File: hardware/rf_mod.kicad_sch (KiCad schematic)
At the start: 170 parts, among them J1001 SMA, J1002 SMA, J1003 Pmod, J101 SMA, J102 SMA, J103 SMA, J1201 SMA, J1202 SMA, J1301 SMA, J1302 SMA, J1303 SMA, J201 SMA, J202 SMA, J401 SMA, J402 SMA, J501 SMA, J502 SMA, J701 SMA, J702 SMA, J703 SMA, J801 SMA, J802 SMA, J803 SMA, J901 USB-C, J902 SMA, Q1001 AO3401A, Q1201 AO3401A, Q1301 AO3401A, Q501 AO3401A, Q701 AO3401A, Q801 AO3401A, SW1001 ON, SW1201 ON, SW1301 ON, SW501 ON, SW701 ON, SW801 ON, U1001 3.3V, U1002 MAX2871, U1201 GALI-84+, U1301 TRF3722, U1302 3.3V, U501 QPL9547, U701 3.3V, U702 ADL5350, U801 3.3V, U802 ADL5350, U901 MT3608, U902 3.3V, U903 74LVC1G17, X901 25 MHz

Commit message: RF-MOD: R1 is a diode-ring mixer (ADEX-10L+, 10-1000 MHz, LO +4 dBm; its baluns and ring of four diodes drawn on the silk) in the splitter's place; R10's RFOUTA- comes out on OUT A- (bottom-right of its right cell) along a 50 ohm line in the margin under the tile, the top pour following it; OUT A becomes OUT A+
Generators: silk drawings (Tile.draw_line / draw_arc), a top-pour tongue below an RF tile (Tile.pour_below), jack names slide up to 4.5 mm and say what blocks them; footprints, symbols and models for the ADEX-10L+ and the HHM22137A1 coupler.

Co-Authored-By: Claude Opus 5.5 <noreply@anthropic.com>
Claude-Session: https://claude.ai/code/session_01RKeoKvFFzjk3cEBLCXXHnB
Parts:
- removed R1006: 5.1k, Resistor_SMD:R_0402_1005Metric, symbol Device:R_US
- removed R101, R102, R103: 18R, Resistor_SMD:R_0402_1005Metric, symbol Device:R_US
- added J1004: Pmod, amod:PinHeader_2x06_P2.54mm_Horizontal_PZ254R-12-12P, symbol Connector_Generic:Conn_02x06_Odd_Even
- added U101: ADEX-10L+, amod:MiniCircuits_CD542_ADEX-10L, symbol amod:ADEX10L
- J1003: value Pmod -> SMA; footprint amod:PinHeader_2x06_P2.54mm_Horizontal_PZ254R-12-12P -> amod:SMA_BWSMA-KE-Z001_Vertical; symbol Connector_Generic:Conn_02x06_Odd_Even -> Connector:Conn_Coaxial; LCSC C492434 -> C496549; MPN PZ254R-12-12P -> BWSMA-KE-Z001
- R1005: value 51R -> 5.1k; LCSC C25125 -> C25905; MPN 0402WGF510JTCE -> 0402WGF5101TCE
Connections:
- net GND: now also J1003.2 (Ext), J1004.3 (Pin_3), J1004.4 (Pin_4), U101.1 (GND), U101.4 (GND), U101.5 (GND); no longer J1003.3 (Pin_3), J1003.4 (Pin_4)
- net PMOD1: now also J1004.12 (Pin_12); no longer J1003.12 (Pin_12)
- net PMOD2: now also J1004.10 (Pin_10); no longer J1003.10 (Pin_10)
- net PMOD3: now also J1004.8 (Pin_8); no longer J1003.8 (Pin_8)
- net PMOD4: now also J1004.6 (Pin_6); no longer J1003.6 (Pin_6)
- net PMOD5: now also J1004.11 (Pin_11); no longer J1003.11 (Pin_11)
- net PMOD6: now also J1004.9 (Pin_9); no longer J1003.9 (Pin_9)
- net PMOD_VCC: now also J1004.1 (Pin_1), J1004.2 (Pin_2); no longer J1003.1 (Pin_1), J1003.2 (Pin_2)
- net R10_RS: now also R1005.1
- net R10_TRM renamed R10_OUTAN
- net R10_OUTAN: now also J1003.1 (In); no longer R1005.1
- net R1_P1 renamed R1_LO
- net R1_LO: now also U101.6 (LO)
- net R1_P2 renamed R1_RF
- net R1_RF: now also U101.3 (RF)
- net R1_P3 renamed R1_IF
- net R1_IF: now also U101.2 (IF)
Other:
- note added: "(+4 dBm, +1 to +7) turns the diodes on in pairs, so the RF is multiplied by +-1 at the LO rate: the IF is RF x square"
- note added: "+4 dBm"
- note added: "-5 dBm"
- note added: "3.3 V and 100 pF: two outputs, 180 degrees apart; put a 50 ohm terminator on one that is unused. RFOUTB is open and must"
- note added: "EXPECT: about 7 dB of conversion loss from 10 MHz to 1 GHz with +4 dBm of LO (R10 at its top power), IF from DC to 800 MHz, 60 dB L-R isolation"
- note added: "EXPECT: any frequency from 23.5 MHz to 6 GHz on OUT A+ and OUT A- (each -4 to +5 dBm in steps, 180 degrees apart), locked to the 25 MHz on REF IN; the red LED says locked"
- note added: "Mini-Circuits ADEX-10L+: two wideband baluns and a ring of four Schottky diodes (drawn beside it on the silk). The LO"
- note added: "OUT A+"
- note added: "OUT A-"
- note added: "R1 diode mixer, ADEX-10L+"
- note added: "REF OUT (51 ohm: 1.6 Vpp into 50 ohm, 3.3 Vpp into a synthesizer's unterminated REF IN; R10's REF IN passes it to R13)."
- note added: "a frequency); 1 dB compression at +1 dBm of RF, IP3 +16 dBm. Compare R7/R8 (ADL5350) and AMOD-A's A9 (MC1496)."
- note added: "and 2.4 GHz (VCO / 2) at ICP 2.56 mA (RSET 5.1 k, CP = 7). RFOUTA+ and RFOUTA- each feed a jack through 27 nH to"
- note added: "stay disabled. CE and RFOUT_EN are tied high, LE has 100 k down. REF IN is unterminated; a back trace takes it on to R13."
- note added: "wave, the sum and difference plus odd LO harmonics. Passive and DC-coupled at IF (a phase detector when RF and LO share"
- note removed: "+20 dBm"
- note removed: "100 pF; RFOUTA- is terminated in 51 ohm the same way; RFOUTB is open and must stay disabled. CE and RFOUT_EN are"
- note removed: "EXPECT: 6.2 dB from any port to either other port, every port within 2 ohm of 50, DC to 6 GHz (the resistors' parasitics set the top)"
- note removed: "EXPECT: any frequency from 23.5 MHz to 6 GHz on OUT A (-4 to +5 dBm in steps), locked to the 25 MHz on REF IN; the red LED says locked"
- note removed: "OUT A"
- note removed: "P1"
- note removed: "P2"
- note removed: "P3"
- note removed: "R1 splitter, 3 x 18 ohm, 6 dB"
- note removed: "REF OUT (51 ohm: 1.6 Vpp into 50 ohm, 3.3 Vpp into a synthesizer's unterminated REF IN; R1 feeds both synthesizers)."
- note removed: "Three 18 ohm resistors to one node: the textbook resistive divider, 6 dB per path and no isolation between the two"
- note removed: "and 2.4 GHz (VCO / 2) at ICP 2.56 mA (RSET 5.1 k, CP = 7). RFOUTA+ feeds the jack through 27 nH to 3.3 V and"
- note removed: "both synthesizers' REF IN, one synthesizer's OUT A to both mixers, or two tones into one gain block."
- note removed: "outputs beyond those 6 dB (a Wilkinson would give 3 dB and 20 dB of isolation, at one band). Feed R9's REF OUT to"
- note removed: "tied high, LE has 100 k down. REF IN is unterminated: one REF OUT drives both synthesizers through R1."
- moved on the sheet: C1011, C1012, C1013, C1014, C1015, J102, J103, R1005

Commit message: Silk case convention on all six boards (Jason, Prompt 17: "To distinguish whole-tile labels from SMA or port labels, use different cases")
Ports (the jacks' names, terminal and loop names, a port named inside a note) stay UPPER CASE.  A tile's label (its
title on the frame, its name in the corner) is Mixed case: the first letter capitalised and the rest as written ("RC
low-pass", "Synthesizer", "I/Q demodulator"; tiles.label_case).  Ranges, values and notes are lower case except units,
acronyms and part numbers ("loss 1.7 dB", "OUT floats").  RF-MOD-2's X1 and X2 take word titles with their chips in
the info; RF-MOD's and RF-MOD-2's LNA tiles are titled "Preamp" ("Low-noise amp" does not fit a cell's frame); a few
two-line labels moved 0.15-0.3 mm for the descenders mixed case brings.  AMOD-P2's tile records (tile_docs), its DOA
list, KIT.md's AMOD-P2 section; X5's calibration points at P14.  All six boards: ERC 0, DRC 0, all fab checks.

Co-Authored-By: Claude Opus 5.5 <noreply@anthropic.com>
Claude-Session: https://claude.ai/code/session_01RKeoKvFFzjk3cEBLCXXHnB
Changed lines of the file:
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@@
 	(wire
 		(pts
+			(xy 370.84 441.96) (xy 365.76 441.96)
+		)
+		(stroke
+			(width 0)
+			(type default)
+		)
+	)
+	(wire
+		(pts
 			(xy 181.61 440.69) (xy 181.61 443.23)
 		)
@@
 	(wire
 		(pts
+			(xy 751.84 314.96) (xy 746.76 314.96)
+		)
+		(stroke
+			(width 0)
+			(type default)
+		)
+	)
+	(wire
+		(pts
 			(xy 167.64 336.55) (xy 170.18 336.55)
 		)
@@
 	(wire
 		(pts
+			(xy 180.34 187.96) (xy 175.26 187.96)
+		)
+		(stroke
+			(width 0)
+			(type default)
+		)
+	)
+	(wire
+		(pts
 			(xy 238.76 236.22) (xy 241.3 236.22)
 		)
@@
 	(wire
 		(pts
-			(xy 365.76 314.96) (xy 370.84 314.96)
-		)
-		(stroke
-			(width 0)
-			(type default)
-		)
-	)
-	(wire
-		(pts
 			(xy 756.92 193.04) (xy 756.92 195.58)
 		)
@@
 	(wire
 		(pts
+			(xy 751.84 187.96) (xy 746.76 187.96)
+		)
+		(stroke
+			(width 0)
+			(type default)
+		)
+	)
+	(wire
+		(pts
 			(xy 156.21 466.09) (xy 153.67 466.09)
 		)
@@
 	(wire
 		(pts
+			(xy 370.84 60.96) (xy 365.76 60.96)
+		)
+		(stroke
+			(width 0)
+			(type default)
+		)
+	)
+	(wire
+		(pts
 			(xy 566.42 66.04) (xy 566.42 68.58)
 		)
@@
 	(wire
 		(pts
+			(xy 345.44 441.96) (xy 340.36 441.96)
+		)
+		(stroke
+			(width 0)
+			(type default)
+		)
+	)
+	(wire
+		(pts
 			(xy 429.26 492.76) (xy 431.8 492.76)
 		)
@@
 	(wire
 		(pts
-			(xy 556.26 60.96) (xy 561.34 60.96)
-		)
-		(stroke
-			(width 0)
-			(type default)
-		)
-	)
-	(wire
-		(pts
 			(xy 519.43 450.85) (xy 521.97 450.85)
 		)
@@
 	(wire
 		(pts
+			(xy 751.84 60.96) (xy 746.76 60.96)
+		)
+		(stroke
+			(width 0)
+			(type default)
+		)
+	)
+	(wire
+		(pts
 			(xy 619.76 353.06) (xy 617.22 353.06)
 		)
@@
 	(wire
 		(pts
-			(xy 365.76 60.96) (xy 370.84 60.96)
-		)
-		(stroke
-			(width 0)
-			(type default)
-		)
-	)
-	(wire
-		(pts
 			(xy 424.18 441.96) (xy 429.26 441.96)
 		)
@@
 	(wire
 		(pts
-			(xy 365.76 187.96) (xy 370.84 187.96)
-		)
-		(stroke
-			(width 0)
-			(type default)
-		)
-	)
-	(wire
-		(pts
 			(xy 528.32 492.76) (xy 525.78 492.76)
 		)
@@
 	(wire
 		(pts
-			(xy 340.36 441.96) (xy 345.44 441.96)
-		)
-		(stroke
-			(width 0)
-			(type default)
-		)
-	)
-	(wire
-		(pts
 			(xy 607.06 500.38) (xy 609.6 500.38)
 		)
@@
 	(wire
 		(pts
-			(xy 175.26 187.96) (xy 180.34 187.96)
-		)
-		(stroke
-			(width 0)
-			(type default)
-		)
-	)
-	(wire
-		(pts
 			(xy 345.44 353.06) (xy 347.98 353.06)
 		)
@@
 	(wire
 		(pts
-			(xy 746.76 187.96) (xy 751.84 187.96)
-		)
-		(stroke
-			(width 0)
-			(type default)
-		)
-	)
-	(wire
-		(pts
 			(xy 190.5 223.52) (xy 193.04 223.52)
 		)
@@
 	(wire
 		(pts
-			(xy 746.76 60.96) (xy 751.84 60.96)
-		)
-		(stroke
-			(width 0)
-			(type default)
-		)
-	)
-	(wire
-		(pts
 			(xy 76.2 223.52) (xy 73.66 223.52)
 		)
@@
 	(wire
 		(pts
-			(xy 746.76 441.96) (xy 751.84 441.96)
-		)
-		(stroke
-			(width 0)
-			(type default)
-		)
-	)
-	(wire
-		(pts
 			(xy 368.3 500.38) (xy 370.84 500.38)
 		)
@@
 	(wire
 		(pts
+			(xy 561.34 60.96) (xy 556.26 60.96)
+		)
+		(stroke
+			(width 0)
+			(type default)
+		)
+	)
+	(wire
+		(pts
 			(xy 685.8 241.3) (xy 683.26 241.3)
 		)
@@
 	(wire
 		(pts
+			(xy 370.84 187.96) (xy 365.76 187.96)
+		)
+		(stroke
+			(width 0)
+			(type default)
+		)
+	)
+	(wire
+		(pts
 			(xy 129.54 199.39) (xy 132.08 199.39)
 		)
@@
 	(wire
 		(pts
+			(xy 370.84 314.96) (xy 365.76 314.96)
+		)
+		(stroke
+			(width 0)
+			(type default)
+		)
+	)
+	(wire
+		(pts
 			(xy 541.02 454.66) (xy 541.02 457.2)
 		)
@@
 	(wire
 		(pts
-			(xy 365.76 441.96) (xy 370.84 441.96)
-		)
-		(stroke
-			(width 0)
-			(type default)
-		)
-	)
-	(wire
-		(pts
 			(xy 535.94 492.76) (xy 538.48 492.76)
 		)
@@
 	(wire
 		(pts
-			(xy 706.12 492.76) (xy 703.58 492.76)
+			(xy 751.84 441.96) (xy 746.76 441.96)
 		)
 		(stroke
@@
 	(wire
 		(pts
-			(xy 429.26 500.38) (xy 431.8 500.38)
+			(xy 706.12 492.76) (xy 703.58 492.76)
 		)
 		(stroke
@@
 	(wire
 		(pts
-			(xy 274.32 223.52) (xy 276.86 223.52)
+			(xy 429.26 500.38) (xy 431.8 500.38)
 		)
 		(stroke
@@
 	(wire
 		(pts
-			(xy 627.38 241.3) (xy 629.92 241.3)
+			(xy 274.32 223.52) (xy 276.86 223.52)
 		)
 		(stroke
@@
 	(wire
 		(pts
-			(xy 520.7 353.06) (xy 518.16 353.06)
+			(xy 627.38 241.3) (xy 629.92 241.3)
 		)
 		(stroke
@@
 	(wire
 		(pts
-			(xy 520.7 254) (xy 518.16 254)
+			(xy 520.7 353.06) (xy 518.16 353.06)
 		)
 		(stroke
@@
 	(wire
 		(pts
-			(xy 449.58 314.96) (xy 454.66 314.96)
+			(xy 520.7 254) (xy 518.16 254)
 		)
 		(stroke
@@
 	(wire
 		(pts
-			(xy 88.9 457.2) (xy 86.36 457.2)
+			(xy 449.58 314.96) (xy 454.66 314.96)
 		)
 		(stroke
@@
 	(wire
 		(pts
-			(xy 746.76 314.96) (xy 751.84 314.96)
+			(xy 88.9 457.2) (xy 86.36 457.2)
 		)
 		(stroke

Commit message: One letter per board, tiles in lower case: AMOD-P2 is AMOD-N (n1-n11), RF-MOD-2 is IQ-MOD (q1-q11), PhMOD's tiles h1-h10
Jason, Prompt 19: "If we can have a nice, well justified single-letter designator for each board, it would make
everything much more clear", and "d11, q11, and c11 don't look like obvious electronics or PCB things".

- p passive, n networks (AMOD-P2's P14, P16-P25), a active, r radio, h PhMOD (Y1-Y10), q quadrature (RF-MOD-2's X1-X11);
  c, m and b are taken for the conversion, motor and brushless boards to come.  PLAN.md section 13 has the table and
  the reasons (no letter moves to another board, no retired name is reused, no s: s11 is the reflection coefficient).
- Every tile name in lower case on the silk, in the code (Tile ids, BACK/BACK_PLOTS/DOCS keys, the nets built on them),
  the handbooks, README, DOA lists, KIT, PLAN and the review brief; pin names (USB-C A1...), the 4046's R1/C1, nets
  named N1/P1, part numbers ending -R7 and the paper size A1 left alone.  tiles.dump refuses a tile not named
  <letter><n>, a number twice, and a BACK key for a tile that does not exist.
- Board and file renames: boards/amod_n.py, boards/iq_mod.py, docs/DOA_amod_n.md, docs/DOA_iq_mod.md, the handbooks,
  the generated hardware, outputs and pictures.  Silk nudged where a lower-case p or q hung onto the line below.
- All six boards rebuilt: ERC 0, DRC 0, every check.

Co-Authored-By: Claude Opus 5.5 <noreply@anthropic.com>
Claude-Session: https://claude.ai/code/session_01RKeoKvFFzjk3cEBLCXXHnB
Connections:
- net R10_AN renamed r10_AN
- net R10_AP renamed r10_AP
- net R10_BF renamed r10_BF
- net R10_CP renamed r10_CP
- net R10_G renamed r10_G
- net R10_LD renamed r10_LD
- net R10_LEDA renamed r10_LEDA
- net R10_N2 renamed r10_N2
- net R10_NF renamed r10_NF
- net R10_OUTA renamed r10_OUTA
- net R10_OUTAN renamed r10_OUTAN
- net R10_REFI renamed r10_REFI
- net R10_REG renamed r10_REG
- net R10_RS renamed r10_RS
- net R10_TN renamed r10_TN
- net R10_V33 renamed r10_V33
- net R10_VS renamed r10_VS
- net R12_G renamed r12_G
- net R12_IN renamed r12_IN
- net R12_IN_A renamed r12_IN_A
- net R12_OUT renamed r12_OUT
- net R12_OUT_A renamed r12_OUT_A
- net R12_VD renamed r12_VD
- net R12_VS renamed r12_VS
- net R13_BBI renamed r13_BBI
- net R13_BBQ renamed r13_BBQ
- net R13_BIN renamed r13_BIN
- net R13_BIP renamed r13_BIP
- net R13_BQN renamed r13_BQN
- net R13_BQP renamed r13_BQP
- net R13_CP renamed r13_CP
- net R13_G renamed r13_G
- net R13_LD renamed r13_LD
- net R13_LEDA renamed r13_LEDA
- net R13_N2 renamed r13_N2
- net R13_REFI renamed r13_REFI
- net R13_RFO renamed r13_RFO
- net R13_RFOUT renamed r13_RFOUT
- net R13_V33 renamed r13_V33
- net R13_VS renamed r13_VS
- net R13_VT renamed r13_VT
- net R1_IF renamed r1_IF
- net R1_LO renamed r1_LO
- net R1_RF renamed r1_RF
- net R2_IN renamed r2_IN
- net R2_OUT renamed r2_OUT
- net R4_IN renamed r4_IN
- net R4_OUT renamed r4_OUT
- net R5_G renamed r5_G
- net R5_IN renamed r5_IN
- net R5_IN_A renamed r5_IN_A
- net R5_OUT renamed r5_OUT
- net R5_OUT_A renamed r5_OUT_A
- net R5_VB renamed r5_VB
- net R5_VS renamed r5_VS
- net R7_G renamed r7_G
- net R7_IF renamed r7_IF
- net R7_IFN renamed r7_IFN
- net R7_LOC renamed r7_LOC
- net R7_LOJ renamed r7_LOJ
- net R7_LON renamed r7_LON
- net R7_RFIF renamed r7_RFIF
- net R7_RFN renamed r7_RFN
- net R7_V33 renamed r7_V33
- net R7_VPOS renamed r7_VPOS
- net R7_VS renamed r7_VS
- net R8_G renamed r8_G
- net R8_IF renamed r8_IF
- net R8_IFN renamed r8_IFN
- net R8_LOC renamed r8_LOC
- net R8_LOJ renamed r8_LOJ
- net R8_LON renamed r8_LON
- net R8_RFIF renamed r8_RFIF
- net R8_RFN renamed r8_RFN
- net R8_V33 renamed r8_V33
- net R8_VPOS renamed r8_VPOS
- net R8_VS renamed r8_VS
- net R9_BUF renamed r9_BUF
- net R9_CC1 renamed r9_CC1
- net R9_CC2 renamed r9_CC2
- net R9_FB renamed r9_FB
- net R9_LEDG renamed r9_LEDG
- net R9_LEDY renamed r9_LEDY
- net R9_OSC renamed r9_OSC
- net R9_REF renamed r9_REF
- net R9_SW renamed r9_SW
- net R9_VBUS renamed r9_VBUS
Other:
- note added: "(0.6 V x 13 from 12 k / 1 k) for the GALI-84+ tile, r12 (100 mA); the +8V rail is a strip under row 1 that their"
- note added: "Both images appear: filter the RF side with r2 or r4."
- note added: "EXPECT: about 7 dB of conversion loss from 10 MHz to 1 GHz with +4 dBm of LO (r10 at its top power), IF from DC to 800 MHz, 60 dB L-R isolation"
- note added: "REF OUT (51 ohm: 1.6 Vpp into 50 ohm, 3.3 Vpp into a synthesizer's unterminated REF IN; r10's REF IN passes it to r13)."
- note added: "Sweep it with r10 or r13 into a power meter, or with a DAC harmonic comb and the ADC."
- note added: "TRF3722 (PLL, VCO, I/Q modulator) on SPI from the Pmod (LE IO6, readback IO5); reference from r10's REF IN. Each DAC:"
- note added: "a frequency); 1 dB compression at +1 dBm of RF, IP3 +16 dBm. Compare r7/r8 (ADL5350) and AMOD-A's a9 (MC1496)."
- note added: "its skirts are much steeper than the LTCC's. Lines, fences and launch voids as on r2."
- note added: "r1 diode mixer, ADEX-10L+"
- note added: "r10 synthesizer, MAX2871"
- note added: "r12 gain block, GALI-84+"
- note added: "r13 I/Q transmitter, TRF3722"
- note added: "r2 2.45 GHz filter"
- note added: "r4 915 MHz filter"
- note added: "r5 LNA, QPL9547"
- note added: "r7 TX mixer, ADL5350"
- note added: "r8 RX mixer, ADL5350"
- note added: "r9 power, USB-C 5 V in: +5, +7.8 V; 25 MHz reference"
- note added: "stay disabled. CE and RFOUT_EN are tied high, LE has 100 k down. REF IN is unterminated; a back trace takes it on to r13."
- note removed: "(0.6 V x 13 from 12 k / 1 k) for the GALI-84+ tile, R12 (100 mA); the +8V rail is a strip under row 1 that their"
- note removed: "Both images appear: filter the RF side with R2 or R4."
- note removed: "EXPECT: about 7 dB of conversion loss from 10 MHz to 1 GHz with +4 dBm of LO (R10 at its top power), IF from DC to 800 MHz, 60 dB L-R isolation"
- note removed: "R1 diode mixer, ADEX-10L+"
- note removed: "R10 synthesizer, MAX2871"
- note removed: "R12 gain block, GALI-84+"
- note removed: "R13 I/Q transmitter, TRF3722"
- note removed: "R2 2.45 GHz filter"
- note removed: "R4 915 MHz filter"
- note removed: "R5 LNA, QPL9547"
- note removed: "R7 TX mixer, ADL5350"
- note removed: "R8 RX mixer, ADL5350"
- note removed: "R9 power, USB-C 5 V in: +5, +7.8 V; 25 MHz reference"
- note removed: "REF OUT (51 ohm: 1.6 Vpp into 50 ohm, 3.3 Vpp into a synthesizer's unterminated REF IN; R10's REF IN passes it to R13)."
- note removed: "Sweep it with R10 or R13 into a power meter, or with a DAC harmonic comb and the ADC."
- note removed: "TRF3722 (PLL, VCO, I/Q modulator) on SPI from the Pmod (LE IO6, readback IO5); reference from R10's REF IN. Each DAC:"
- note removed: "a frequency); 1 dB compression at +1 dBm of RF, IP3 +16 dBm. Compare R7/R8 (ADL5350) and AMOD-A's A9 (MC1496)."
- note removed: "its skirts are much steeper than the LTCC's. Lines, fences and launch voids as on R2."
- note removed: "stay disabled. CE and RFOUT_EN are tied high, LE has 100 k down. REF IN is unterminated; a back trace takes it on to R13."

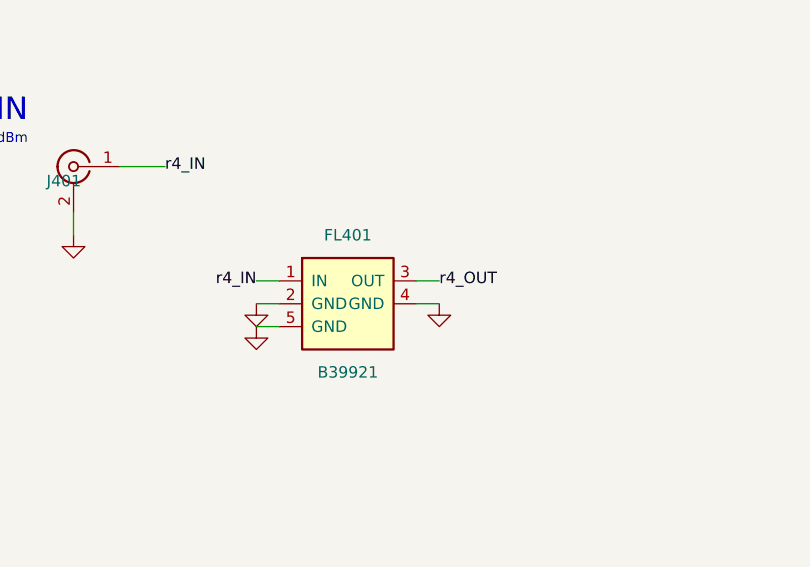
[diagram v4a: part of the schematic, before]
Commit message: Two pinouts read against their datasheets and fixed: the DMMT3904W (AMOD-C's c9 and c10) is 1 B2, 2 B1, 3 C1, 4 E1, 5 E2, 6 C2, not the BCM857BS's order (c9's pair turned 180 with IN+ under it on the back, c10's turned 180 with Q1's base on the back); RF-MOD's 915 MHz SAW has its output on pad 4, not 3 (r4 took it from a ground pad). scripts/check_pinouts.py compares every symbol's pin names with EasyEDA's: these two were its only real disagreements
Co-Authored-By: Claude Opus 5.5 <noreply@anthropic.com>
Claude-Session: https://claude.ai/code/session_01RKeoKvFFzjk3cEBLCXXHnB
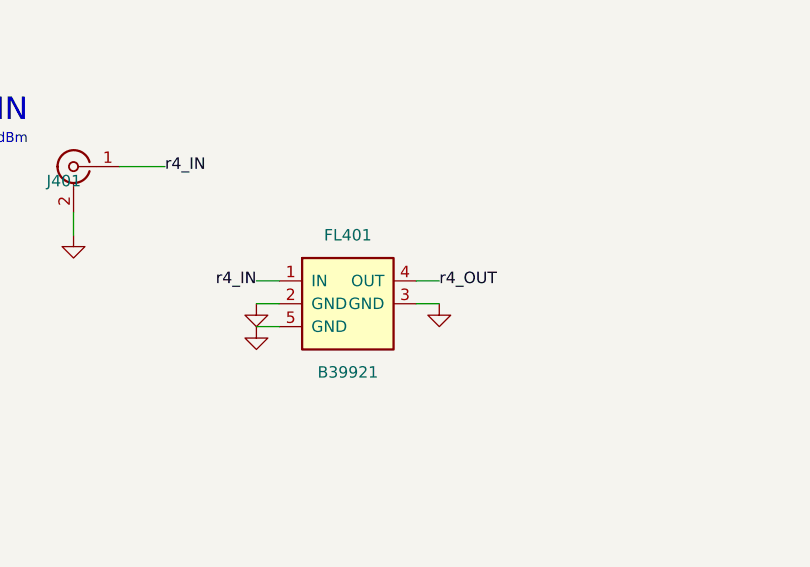
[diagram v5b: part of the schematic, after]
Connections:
- net GND: now also FL401.3 (GND); no longer FL401.4 (GND)
- net r4_OUT: now also FL401.4 (OUT); no longer FL401.3 (OUT)
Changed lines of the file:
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@@
 		(pin "5"
+		)
+		(pin "4"
 		)
 		(pin "3"
 		)
-		(pin "4"
-		)
 		(instances
